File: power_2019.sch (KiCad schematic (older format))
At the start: 30 parts, among them J2 Alim puissance, J3 Alim logique, Q1 PMF370XN, Q2 2N7000, Q3 PMF370XN, Q4 PMF370XN, U1 TC1262-33, U3 servo_connector

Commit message: maj
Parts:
- removed D1: LED_hardfault_jaune, LED_SMD:LED_1206_3216Metric_Pad1.42x1.75mm_HandSolder, symbol Device:LED
- removed D2: LED_communication_vert, LED_SMD:LED_1206_3216Metric_Pad1.42x1.75mm_HandSolder, symbol Device:LED
- removed D3: led_feedback_vert, LED_SMD:LED_1206_3216Metric_Pad1.42x1.75mm_HandSolder, symbol Device:LED
- removed Q1, Q3, Q4: PMF370XN, Package_TO_SOT_SMD:SOT-323_SC-70_Handsoldering, symbol Device:Q_NMOS_GSD
- removed R1, R4, R5: 150, Resistor_SMD:R_1206_3216Metric_Pad1.42x1.75mm_HandSolder, symbol Device:R
- removed U3: servo_connector, @Robot:HE14-4-straight, symbol @Robot:servo_connector
- removed U?: LM2576S-5, Package_TO_SOT_SMD:TO-263-5_TabPin3, symbol Regulator_Switching:LM2576S-5
- added 1000µF? (x2): CP, symbol Device:CP
- added 100µH? (x2): L, symbol Device:L
- added C? (x2): 470µ, symbol Device:CP
- added D? (x2): LED, symbol Device:LED
- added D? (x2): 1N5822, Diode_THT:D_DO-201AD_P15.24mm_Horizontal, symbol Diode:1N5822
- added F? (x2): Fuse, symbol Device:Fuse
- added J?: Conn_Servo, symbol Connector:Conn_01x04_Male
- added J?: Conn_Moteur, symbol Connector:Conn_01x02_Male
- added J?: Conn_Power_IN, symbol Connector:Conn_01x04_Female
- added J?: Conn_Power_OUT, symbol Connector:Conn_01x04_Female
- added J?: Conn_5V, symbol Connector:Conn_01x02_Male
- added R? (x3): 11.5k, symbol Device:R
- added R? (x3): 2.26k, symbol Device:R
- added R? (x2): 350, symbol Device:R
- added U? (x3): LM2576T-ADJ, Package_TO_SOT_THT:TO-220-5_Vertical, symbol Regulator_Switching:LM2576T-ADJ
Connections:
- net +5V: now also 1000µF?.1, 100µH?.2, J?.1 (Pin_1), R?.1, R?.1; no longer 1000µF.1, 100µH.2, R?.1
- net +BATT: now also F?.2, F?.2
- net GND: now also J?.1 (Pin_1), J?.1 (Pin_1)
- net +12V: now reaches C?.1, F?.2, R?.1
- net +12V: now also J?.2 (Pin_2)
- net at C?.1, F?.1: now also U?.1 (VIN)
- net at 1000µF.2, C?.2, D?.1 (K)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: now also U?.3 (GND), U?.5 (~ON~/OFF)
- net at 100µH.1, D?.1 (K): now also U?.2 (OUT)
- new net: R?.1, R?.2, U?.4 (FB) (x3)
- new net: C?.1, F?.1, U?.1 (VIN) (x2)
- new net: 1000µF?.2, C?.2, D?.1 (K), D?.2 (A), U?.3 (GND), U?.5 (~ON~/OFF) (x2)
- new net: D?.2 (A), R?.2 (x2)
- new net: 100µH?.1, D?.1 (K), U?.2 (OUT) (x2)
- new net +7.5V: 1000µF.1, 1000µF?.1, 100µH.2, 100µH?.2, J?.3 (Pin_3), R?.1, R?.1, R?.1, R?.1
- new net 12V_OUT: J?.2 (Pin_2), J?.2 (Pin_2)
- new net 5V_OUT: J?.1 (Pin_1), J?.2 (Pin_2)
- new net 7.4V_OUT: J?.3 (Pin_3)
- new net Servo1: J?.4 (Pin_4)
- new net Servo2: J?.3 (Pin_3)
- no-connect marks 7 -> 1
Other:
- note added: "Regu 5V\n\n"
- note added: "Regu 7.4V\n"
- note removed: "Led"
- note removed: "Regu 5V"
- note removed: "input : 3.3v ou 5v"
- note removed: "ne pas conecter\nle vcc"
- moved on the sheet: 1000µF, 100µH, C?, D?, F?, R?

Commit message: update power board
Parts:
- removed 1000µF?: CP, symbol Device:CP
- removed 100µH?: L, symbol Device:L
- removed C1, C2: 1u, Capacitor_SMD:C_1206_3216Metric_Pad1.42x1.75mm_HandSolder, symbol Device:C
- removed C?: 470µ, symbol Device:CP
- removed D?: LED, symbol Device:LED
- removed D?: 1N5822, Diode_THT:D_DO-201AD_P15.24mm_Horizontal, symbol Diode:1N5822
- removed F?: Fuse, symbol Device:Fuse
- removed J3: Alim logique, @Robot:HE14-3_horizontal, symbol Connector_Generic:Conn_01x03
- removed J?: Conn_Servo, symbol Connector:Conn_01x04_Male
- removed J?: Conn_Moteur, symbol Connector:Conn_01x02_Male
- removed J?: Conn_Power_IN, symbol Connector:Conn_01x04_Female
- removed J?: Conn_Power_OUT, symbol Connector:Conn_01x04_Female
- removed J?: Conn_5V, symbol Connector:Conn_01x02_Male
- removed Q2: 2N7000, Package_TO_SOT_THT:TO-92_Inline, symbol Transistor_FET:2N7000
- removed R2, R3: 10k, Resistor_SMD:R_1206_3216Metric_Pad1.42x1.75mm_HandSolder, symbol Device:R
- removed R?: 350, symbol Device:R
- removed R?: 11.5k, symbol Device:R
- removed R?: 2.26k, symbol Device:R
- removed U1: TC1262-33, Package_TO_SOT_SMD:SOT-223-3_TabPin2, symbol Regulator_Linear:TC1262-33
- removed U?: LM2576T-ADJ, Package_TO_SOT_THT:TO-220-5_Vertical, symbol Regulator_Switching:LM2576T-ADJ
- added C? (x2): 100u, symbol Device:CP
- added D?: D, symbol Device:D
- added F?: Fuse, symbol Device:Fuse
- added J?: Alim logique, @Robot:HE14-2-straight, symbol Connector_Generic:Conn_01x02
- added J?: Conn_SERVO, symbol Connector_Generic:Conn_01x04
- added J?: Conn_Sortie_VersFacade, symbol Connector_Generic:Conn_01x04
- added J?: Conn_Entree_DepuisFacade, symbol Connector_Generic:Conn_01x04
- added J?: Alim_5V, symbol Connector_Generic:Conn_01x02
- added J?: Alim_12V, symbol Connector_Generic:Conn_01x02
- added R?: 353, symbol Device:R
- added U?: PTH08080W, @Robot_symbols:PTH08080W, symbol pth08080:PTH08080W
- R?: value 11.5k -> 9.255k
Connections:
- net +12V: now also J?.2 (Pin_2)
- net +5V: now also C?.1, D?.2 (A), J?.1 (Pin_1), J?.2 (Pin_2), U?.3 (VO)
- net +7.5V: now also J?.3 (Pin_3)
- net +BATT: now also F?.2
- net 12V_OUT: now also J?.1 (Pin_1), J?.2 (Pin_2)
- net 5V_OUT: now also J?.1 (Pin_1), J?.1 (Pin_1)
- net 7.4V_OUT: now also J?.3 (Pin_3)
- net GND: now also 1000µF.2, 1000µF?.2, C?.2, C?.2, D?.1 (K), D?.1 (K), D?.2 (A), D?.2 (A), U?.3 (GND), U?.3 (GND), U?.5 (~ON~/OFF), U?.5 (~ON~/OFF), C?.2, C?.2, J?.1 (Pin_1), J?.2 (Pin_2), J?.2 (Pin_2), R?.2, U?.2 (GND)
- new net: C?.1, D?.1 (K), F?.1, U?.1 (VI)
- new net: R?.1, U?.4 (ADJ)
- new net 7,4V: J?.2 (Pin_2)
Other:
- note added: "R : 0.05W tolerant with temperaturestability of 100 ppm/°C"
- note added: "SORTIE 5 V\n"
- note removed: "Regu 5V\n\n"
- note removed: "détrompeur"
- note removed: "logic level converter"

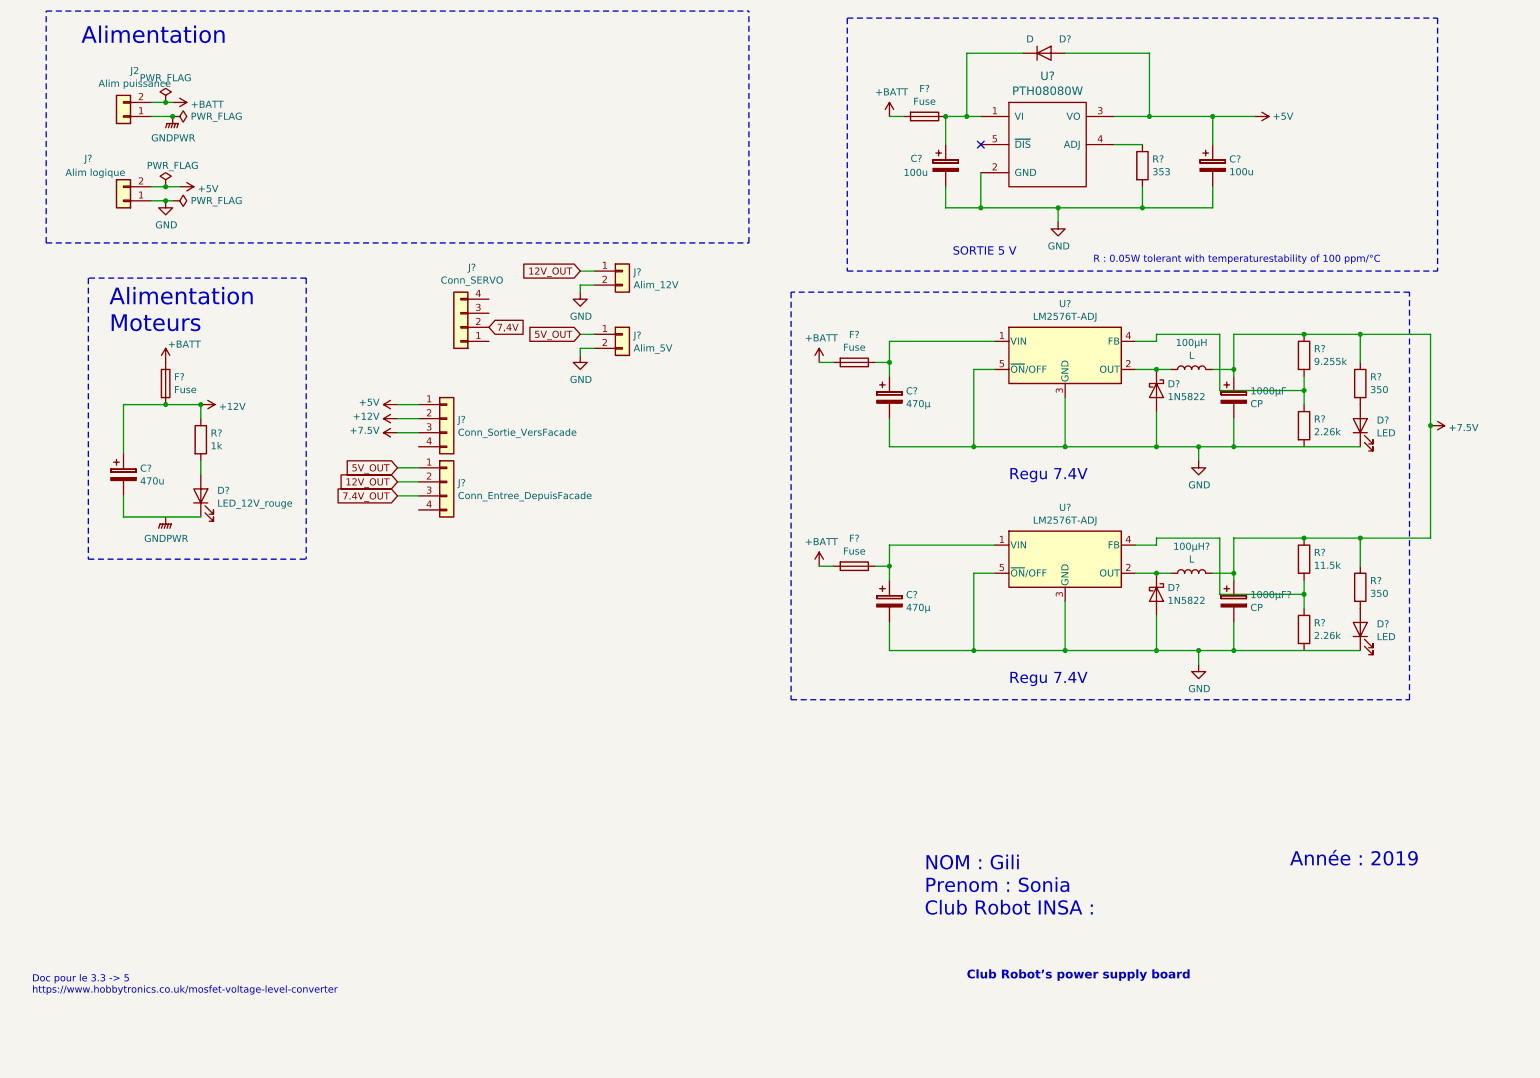
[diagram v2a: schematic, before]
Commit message: update power board
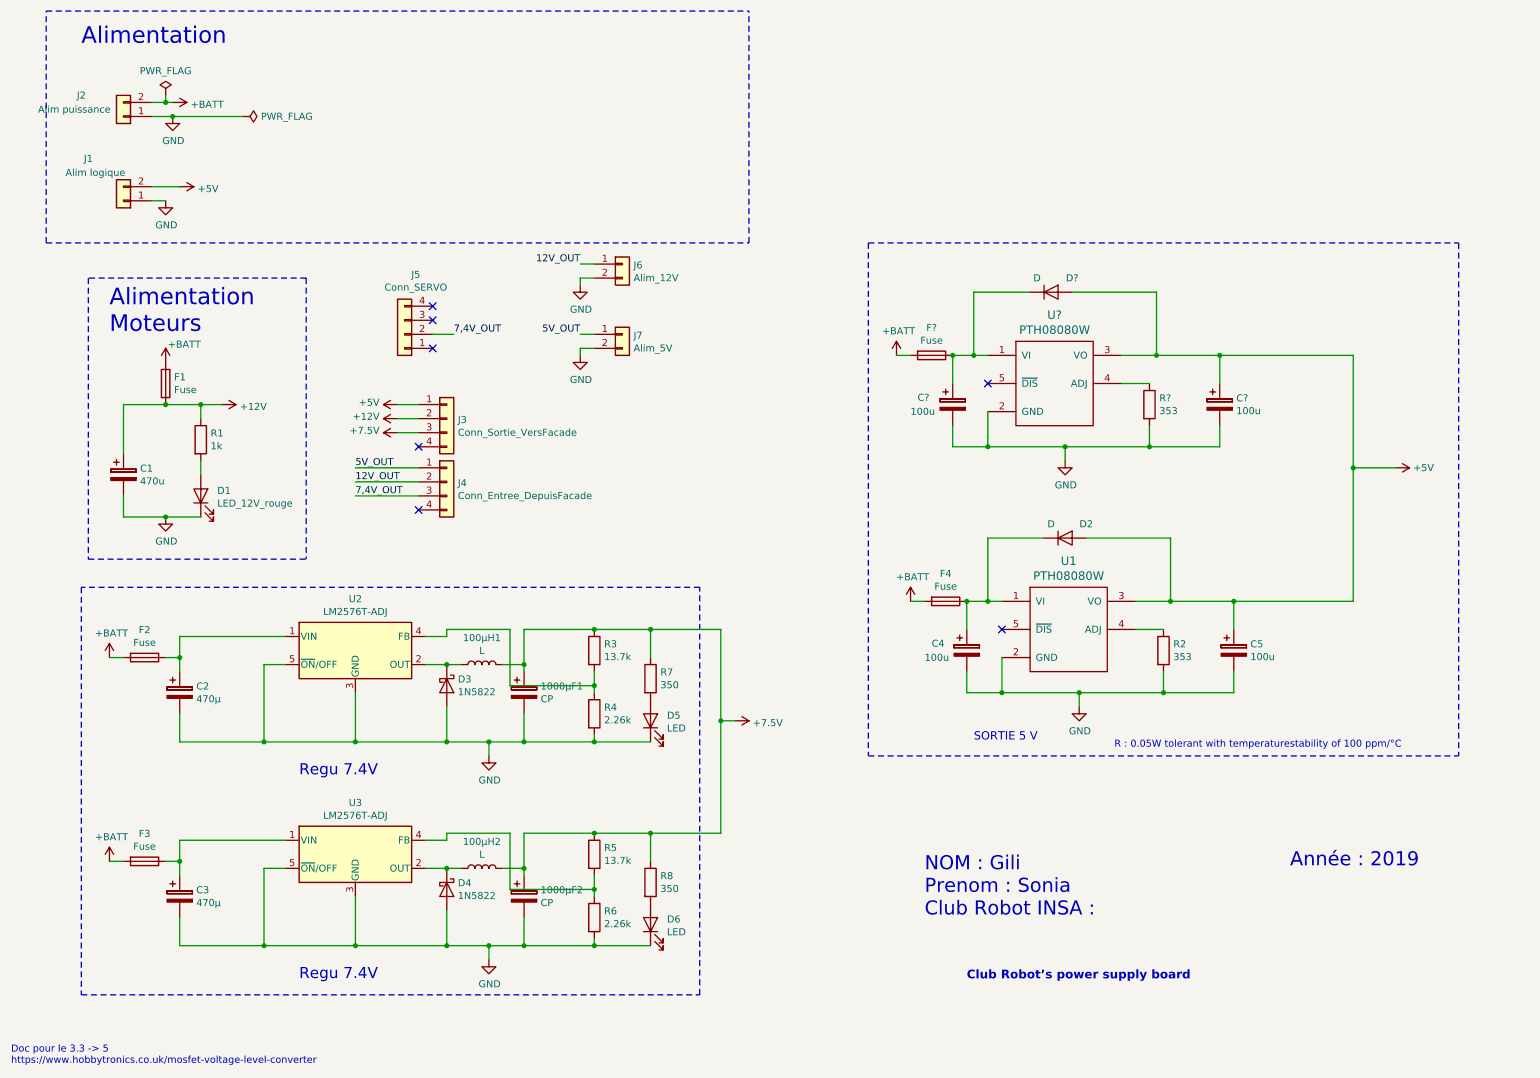
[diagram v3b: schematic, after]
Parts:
- added C? (x2): 100u, symbol Device:CP
- added D?: D, symbol Device:D
- added F?: Fuse, symbol Device:Fuse
- added R?: 353, symbol Device:R
- added U?: PTH08080W, @Robot_symbols:PTH08080W, symbol pth08080:PTH08080W
- J1: renamed from J?; footprint @Robot:HE14-2-straight -> TerminalBlock_Phoenix:TerminalBlock_Phoenix_MPT-0,5-2-2.54_1x02_P2.54mm_Horizontal
- J2: footprint @Robot:HE14-2-straight -> TerminalBlock_Phoenix:TerminalBlock_Phoenix_MPT-0,5-2-2.54_1x02_P2.54mm_Horizontal
- R3: renamed from R?; value 9.255k -> 13.7k
- R5: renamed from R?; value 11.5k -> 13.7k
- gave numbers to parts that had none: 31
- renumbered 1000µF to 1000µF1, 100µH to 100µH1
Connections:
- net 7.4V_OUT is gone; now on net 7,4V_OUT: J4.3 (Pin_3)
- net GNDPWR is gone; now on net GND: J2.1 (Pin_1)
- net +5V: now also C?.1, D?.2 (A), U?.3 (VO)
- net +BATT: now also F?.2
- net GND: now also C1.2, D1.1 (K), R4.2, R6.2, C?.2, C?.2, R?.2, U?.2 (GND)
- net 7,4V renamed 7,4V_OUT
- new net: C?.1, D?.1 (K), F?.1, U?.1 (VI)
- new net: R?.1, U?.4 (ADJ)
- no-connect marks 1 -> 7
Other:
- moved on the sheet: 1000µF1, 1000µF2, 100µH1, 100µH2, C2, C3, C4, C5, D2, D3, D4, D5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

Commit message: alim moteur
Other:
- note added: "Attention: montage incorrecte, ne pas mettre les régus en parallèle\n"
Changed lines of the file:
@@
 EESchema Schematic File Version 4
+LIBS:power_2019-cache
 EELAYER 26 0
 EELAYER END
@@
 Wire Notes Line
 	10850 2250 10850 5900
+Text Notes 8100 850  0    50   ~ 0
+Attention: montage incorrecte, ne pas mettre les régus en parallèle\n
 $EndSCHEMATC
